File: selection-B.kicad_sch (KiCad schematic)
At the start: 5 parts, among them U14 74LS08, U15 74LS32, U16 74LS08, U17 74LS08, U18 74HC04

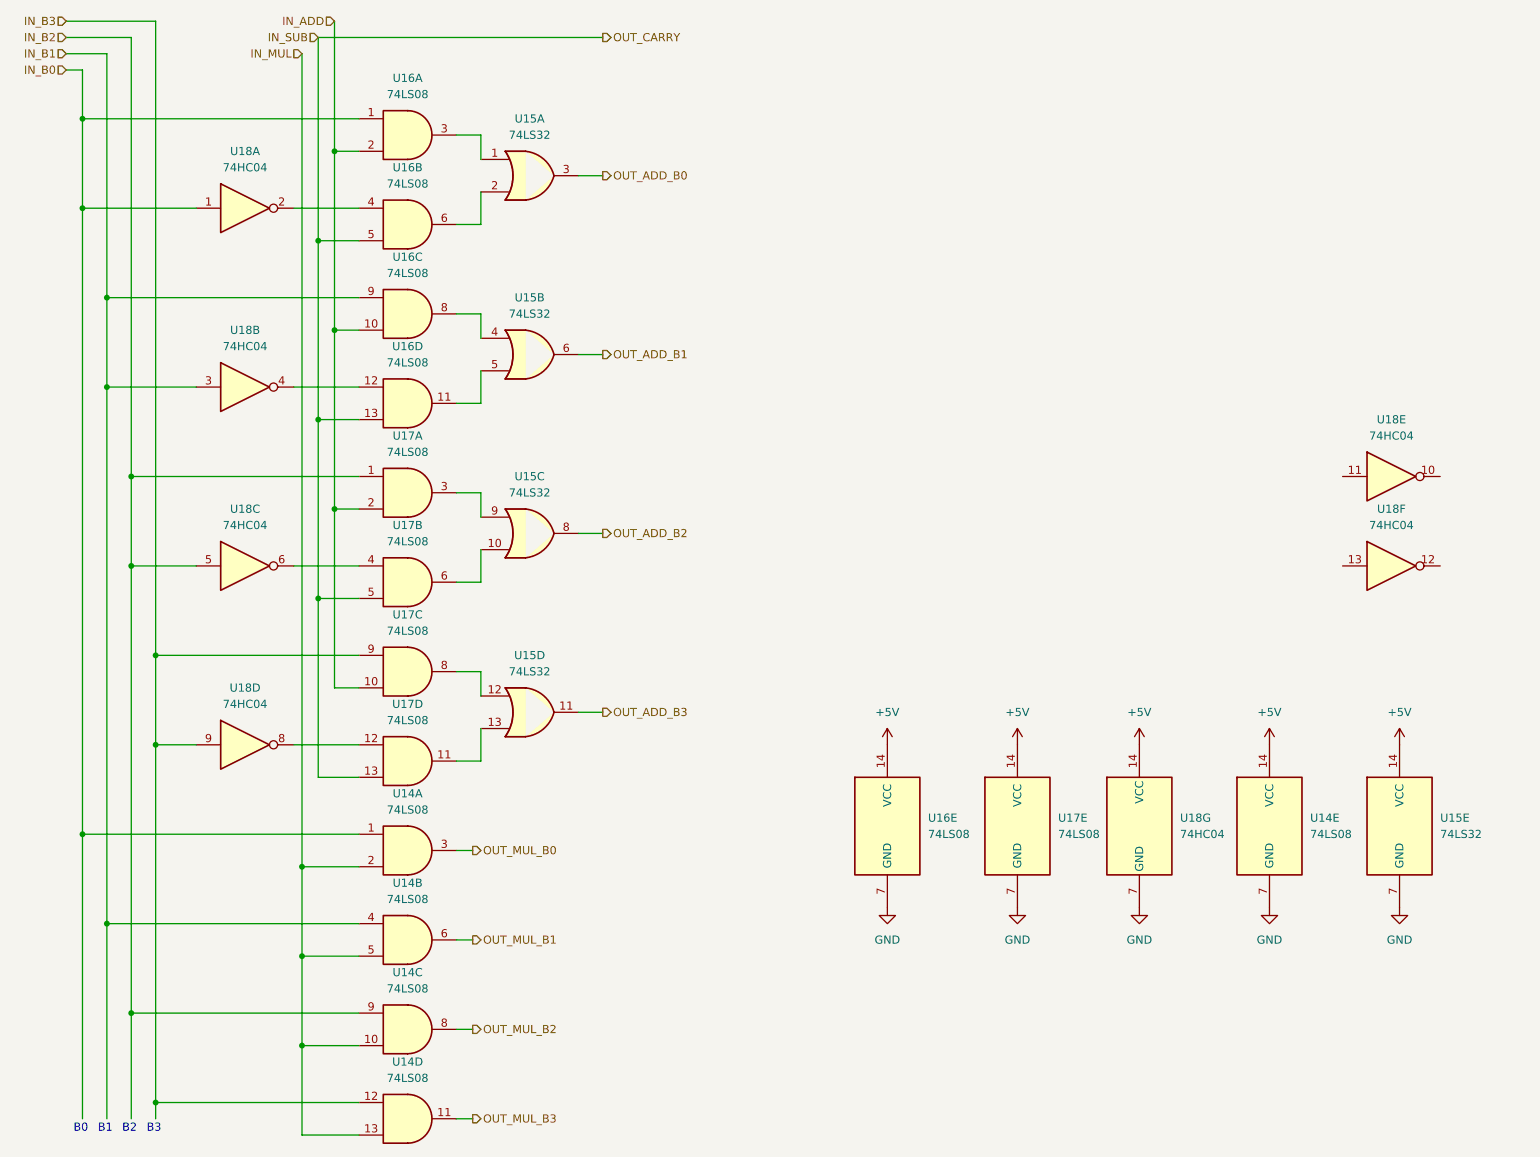
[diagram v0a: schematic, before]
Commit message: feat: removed ERC errors
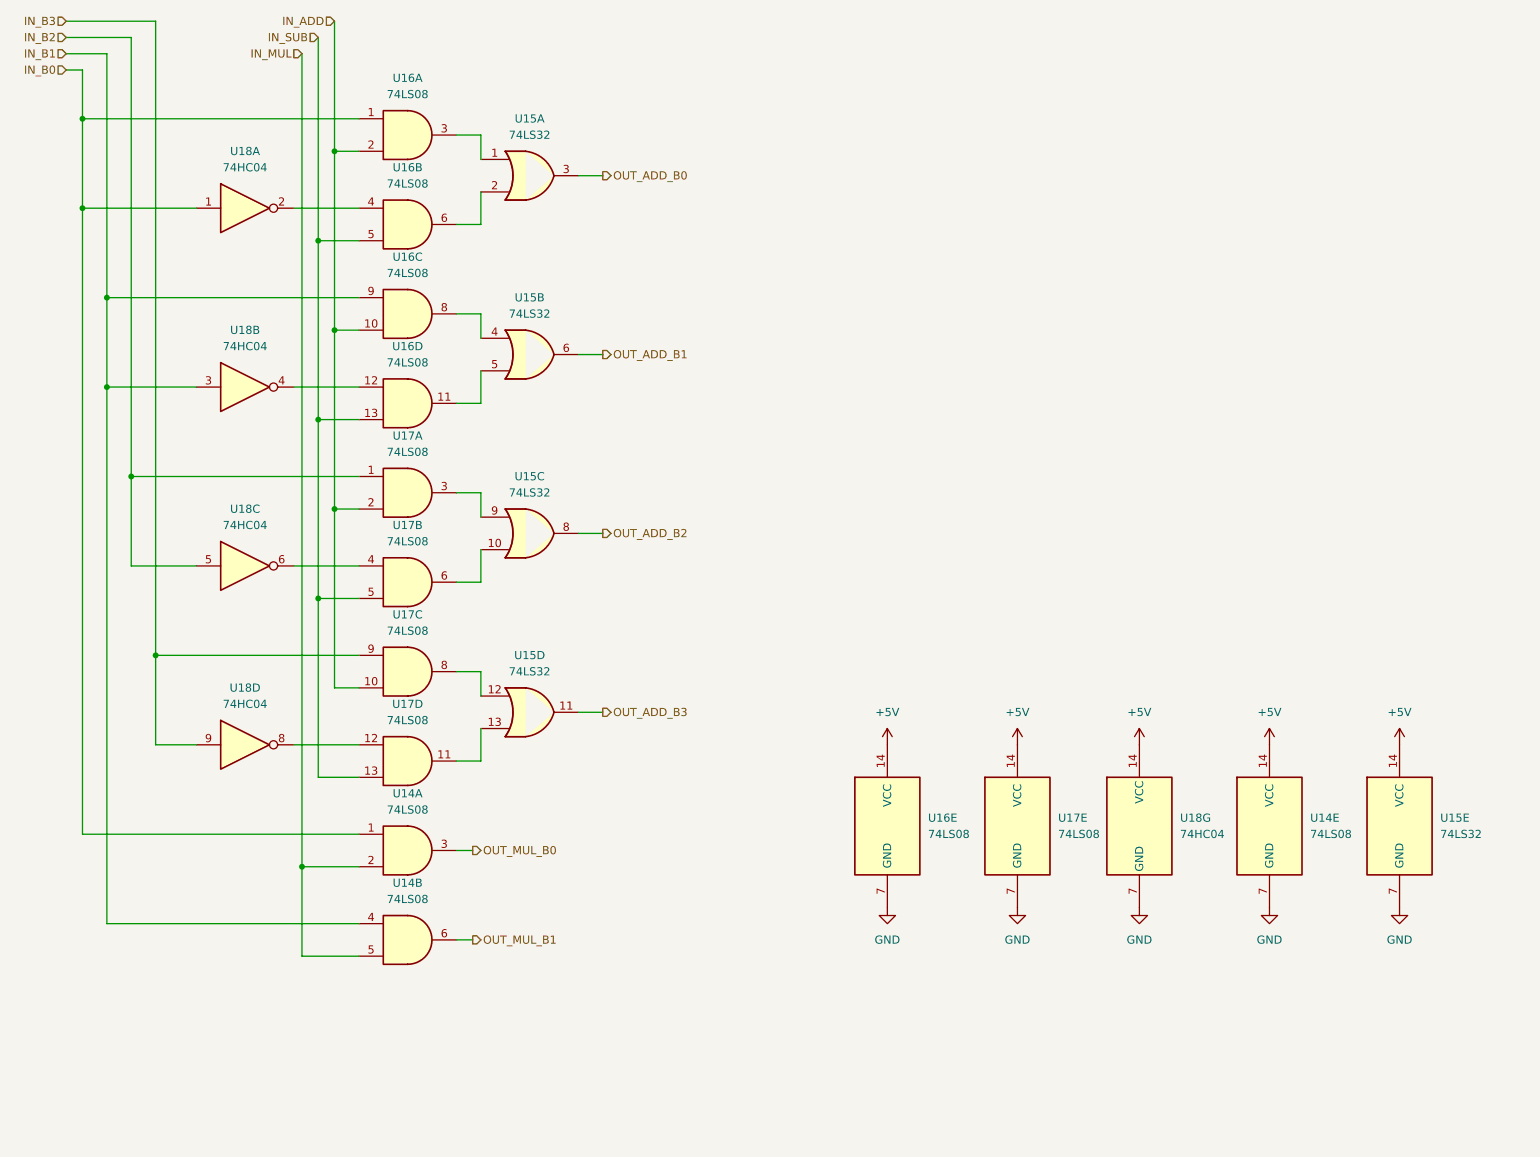
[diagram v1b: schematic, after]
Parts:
- removed unit 4 of U14
- removed unit 3 of U14
- removed unit 6 of U18
- removed unit 5 of U18
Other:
- note removed: "B0"
- note removed: "B1"
- note removed: "B2"
- note removed: "B3"

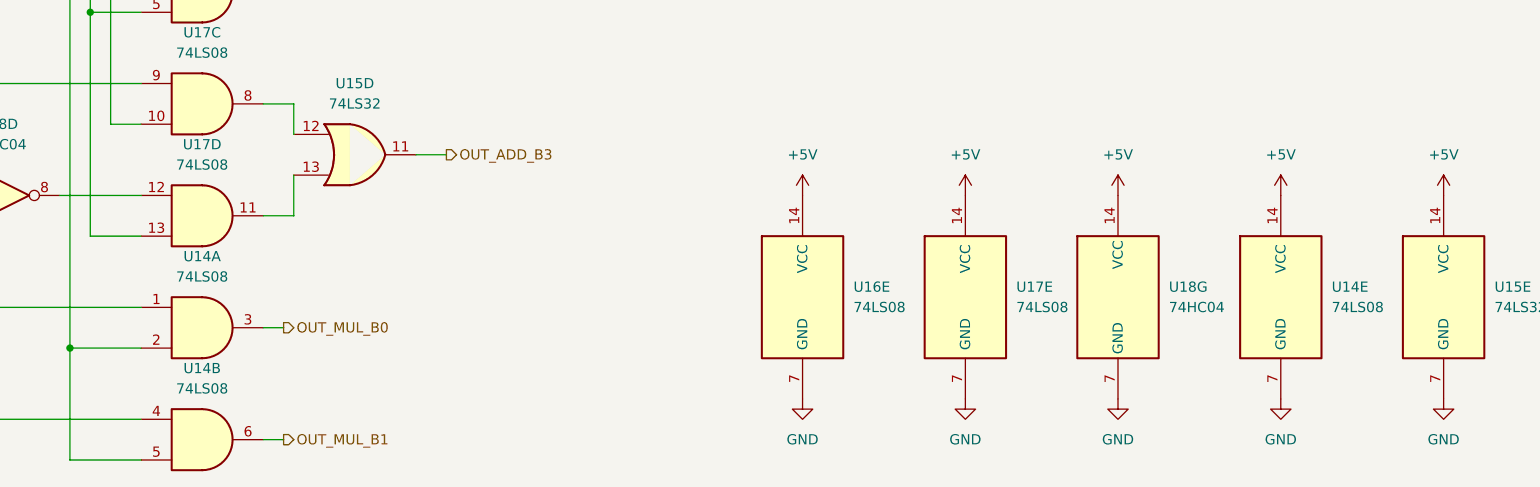
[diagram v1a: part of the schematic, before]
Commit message: fix: removed ERC warnings and errors
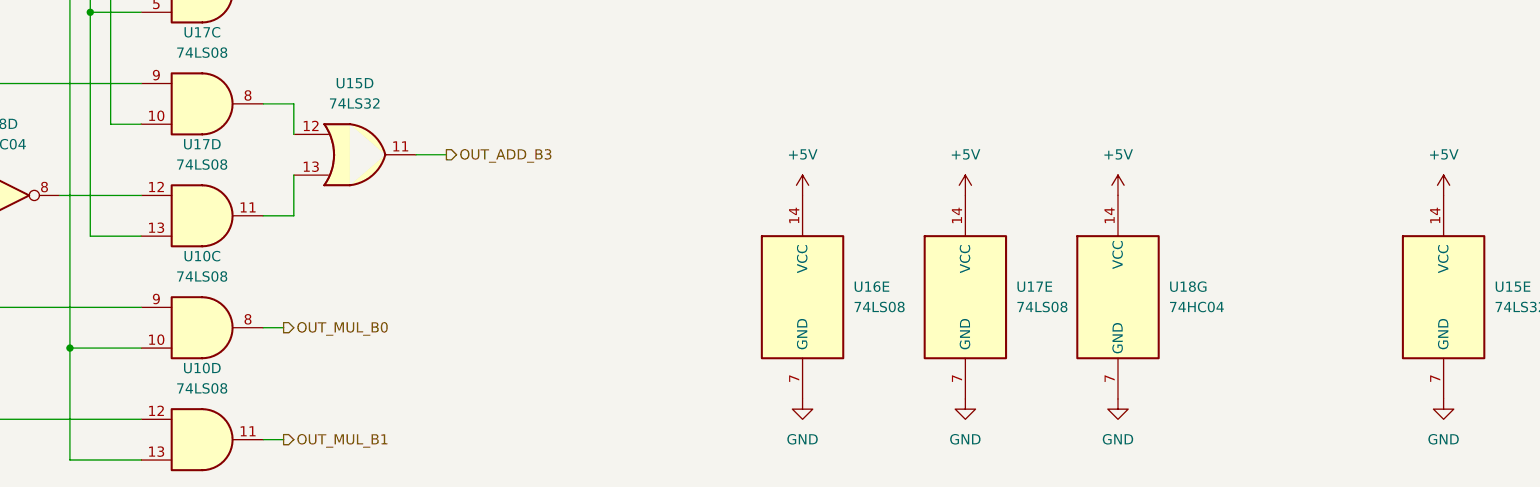
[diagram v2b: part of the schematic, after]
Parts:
- removed unit 5 of U14
- renumbered U14 to U10
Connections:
- net IN_B0: now also U10.9; no longer U10.1
- net IN_B1: now also U10.12; no longer U10.4
- net IN_MUL: now also U10.10, U10.13; no longer U10.2, U10.5
- net OUT_MUL_B0: now also U10.8; no longer U10.3
- net OUT_MUL_B1: now also U10.11; no longer U10.6
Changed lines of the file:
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@@
 		(lib_id "74xx:74LS08")
 		(at 113.03 161.29 0)
-		(unit 2)
-		(exclude_from_sim no)
-		(in_bom yes)
-		(on_board yes)
-		(dnp no)
-		(fields_autoplaced yes)
-		(property "Reference" "U14"
+		(unit 4)
+		(exclude_from_sim no)
+		(in_bom yes)
+		(on_board yes)
+		(dnp no)
+		(fields_autoplaced yes)
+		(property "Reference" "U10"
 			(at 113.0217 152.4 0)
 			(effects
@@
 			(project ""
 				(path "/4987240f-8890-46b8-b8e9-0d60580cb205/e08b8046-a666-4685-8ce4-06ee0f7f0287"
-					(reference "U14")
-					(unit 2)
+					(reference "U10")
+					(unit 4)
 				)
 			)
@@
 		(lib_id "74xx:74LS08")
 		(at 113.03 147.32 0)
-		(unit 1)
-		(exclude_from_sim no)
-		(in_bom yes)
-		(on_board yes)
-		(dnp no)
-		(fields_autoplaced yes)
-		(property "Reference" "U14"
+		(unit 3)
+		(exclude_from_sim no)
+		(in_bom yes)
+		(on_board yes)
+		(dnp no)
+		(fields_autoplaced yes)
+		(property "Reference" "U10"
 			(at 113.0217 138.43 0)
 			(effects
@@
 			(project ""
 				(path "/4987240f-8890-46b8-b8e9-0d60580cb205/e08b8046-a666-4685-8ce4-06ee0f7f0287"
-					(reference "U14")
-					(unit 1)
-				)
-			)
-		)
-	)
-	(symbol
-		(lib_id "74xx:74LS08")
-		(at 247.65 143.51 0)
-		(unit 5)
-		(exclude_from_sim no)
-		(in_bom yes)
-		(on_board yes)
-		(dnp no)
-		(fields_autoplaced yes)
-		(property "Reference" "U14"
-			(at 254 142.2399 0)
-			(effects
-				(font
-					(size 1.27 1.27)
-				)
-				(justify left)
-			)
-		)
-		(property "Value" "74LS08"
-			(at 254 144.7799 0)
-			(effects
-				(font
-					(size 1.27 1.27)
-				)
-				(justify left)
-			)
-		)
-		(property "Footprint" ""
-			(at 247.65 143.51 0)
-			(effects
-				(font
-					(size 1.27 1.27)
-				)
-				(hide yes)
-			)
-		)
-		(property "Datasheet" "http://www.ti.com/lit/gpn/sn74LS08"
-			(at 247.65 143.51 0)
-			(effects
-				(font
-					(size 1.27 1.27)
-				)
-				(hide yes)
-			)
-		)
-		(property "Description" "Quad And2"
-			(at 247.65 143.51 0)
-			(effects
-				(font
-					(size 1.27 1.27)
-				)
-				(hide yes)
-			)
-		)
-		(pin "2"
-		)
-		(pin "12"
-		)
-		(pin "9"
-		)
-		(pin "7"
-		)
-		(pin "11"
-		)
-		(pin "13"
-		)
-		(pin "1"
-		)
-		(pin "10"
-		)
-		(pin "14"
-		)
-		(pin "8"
-		)
-		(pin "4"
-		)
-		(pin "3"
-		)
-		(pin "6"
-		)
-		(pin "5"
-		)
-		(instances
-			(project ""
-				(path "/4987240f-8890-46b8-b8e9-0d60580cb205/e08b8046-a666-4685-8ce4-06ee0f7f0287"
-					(reference "U14")
-					(unit 5)
+					(reference "U10")
+					(unit 3)
 				)
 			)
@@
 	)
 	(symbol
-		(lib_id "power:+5V")
-		(at 247.65 130.81 0)
-		(unit 1)
-		(exclude_from_sim no)
-		(in_bom yes)
-		(on_board yes)
-		(dnp no)
-		(fields_autoplaced yes)
-		(property "Reference" "#PWR028"
-			(at 247.65 134.62 0)
-			(effects
-				(font
-					(size 1.27 1.27)
-				)
-				(hide yes)
-			)
-		)
-		(property "Value" "+5V"
-			(at 247.65 125.73 0)
-			(effects
-				(font
-					(size 1.27 1.27)
-				)
-			)
-		)
-		(property "Footprint" ""
-			(at 247.65 130.81 0)
-			(effects
-				(font
-					(size 1.27 1.27)
-				)
-				(hide yes)
-			)
-		)
-		(property "Datasheet" ""
-			(at 247.65 130.81 0)
-			(effects
-				(font
-					(size 1.27 1.27)
-				)
-				(hide yes)
-			)
-		)
-		(property "Description" "Power symbol creates a global label with name \"+5V\""
-			(at 247.65 130.81 0)
-			(effects
-				(font
-					(size 1.27 1.27)
-				)
-				(hide yes)
-			)
-		)
-		(pin "1"
-		)
-		(instances
-			(project ""
-				(path "/4987240f-8890-46b8-b8e9-0d60580cb205/e08b8046-a666-4685-8ce4-06ee0f7f0287"
-					(reference "#PWR028")
-					(unit 1)
-				)
-			)
-		)
-	)
-	(symbol
 		(lib_id "74xx:74LS32")
 		(at 132.08 69.85 0)
@@
 				)
 			)
-		)
-	)
-	(symbol
-		(lib_id "power:GND")
-		(at 247.65 156.21 0)
-		(unit 1)
-		(exclude_from_sim no)
-		(in_bom yes)
-		(on_board yes)
-		(dnp no)
-		(fields_autoplaced yes)
-		(property "Reference" "#PWR033"
-			(at 247.65 162.56 0)
-			(effects
-				(font
-					(size 1.27 1.27)
-				)
-				(hide yes)
-			)
-		)
-		(property "Value" "GND"
-			(at 247.65 161.29 0)
-			(effects
-				(font
-					(size 1.27 1.27)
-				)
-			)
-		)
-		(property "Footprint" ""
-			(at 247.65 156.21 0)
-			(effects
-				(font
-					(size 1.27 1.27)
-				)
-				(hide yes)
-			)
-		)
-		(property "Datasheet" ""
-			(at 247.65 156.21 0)
-			(effects
-				(font
-					(size 1.27 1.27)
-				)
-				(hide yes)
-			)
-		)
-		(property "Description" "Power symbol creates a global label with name \"GND\" , ground"
-			(at 247.65 156.21 0)
-			(effects
-				(font
-					(size 1.27 1.27)
-				)
-				(hide yes)
-			)
-		)
-		(pin "1"
-		)
-		(instances
-			(project ""
-				(path "/4987240f-8890-46b8-b8e9-0d60580cb205/e08b8046-a666-4685-8ce4-06ee0f7f0287"
-					(reference "#PWR033")
-					(unit 1)
-				)
-			)

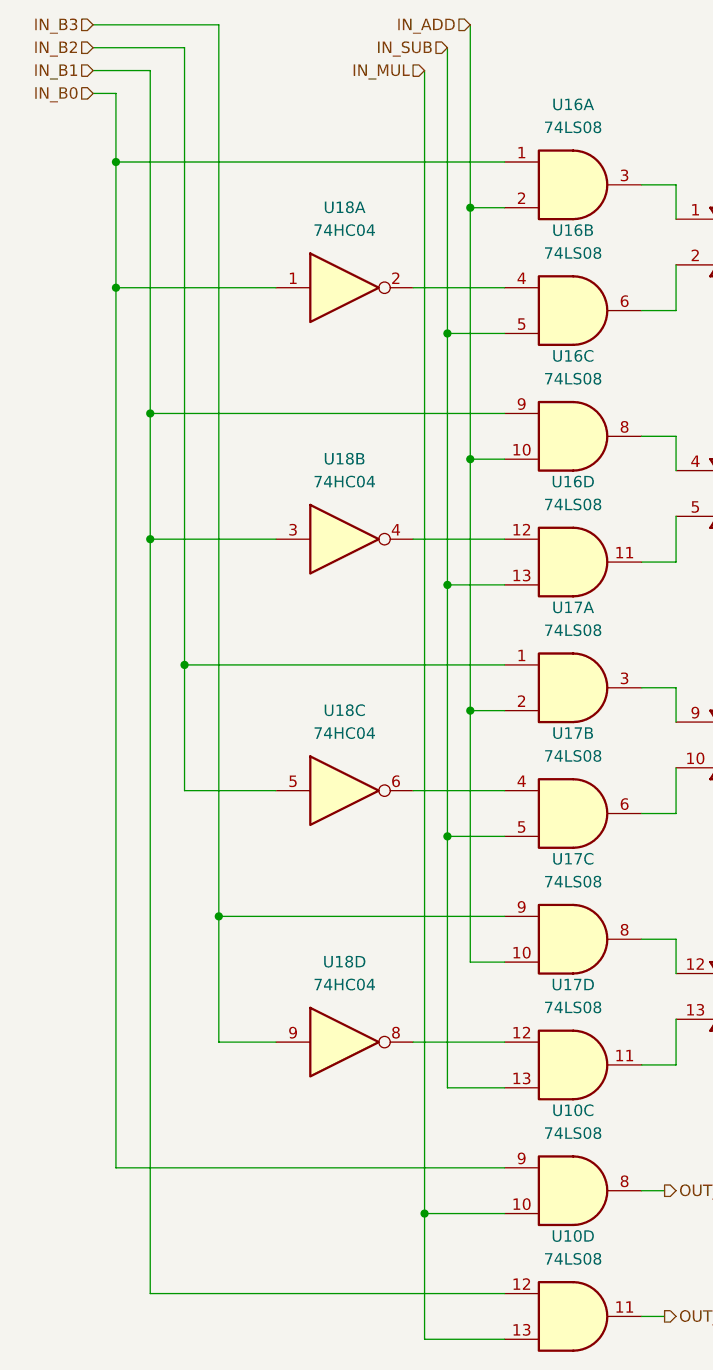
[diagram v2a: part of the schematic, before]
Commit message: feat: NOT to mofset + first batch of footprint
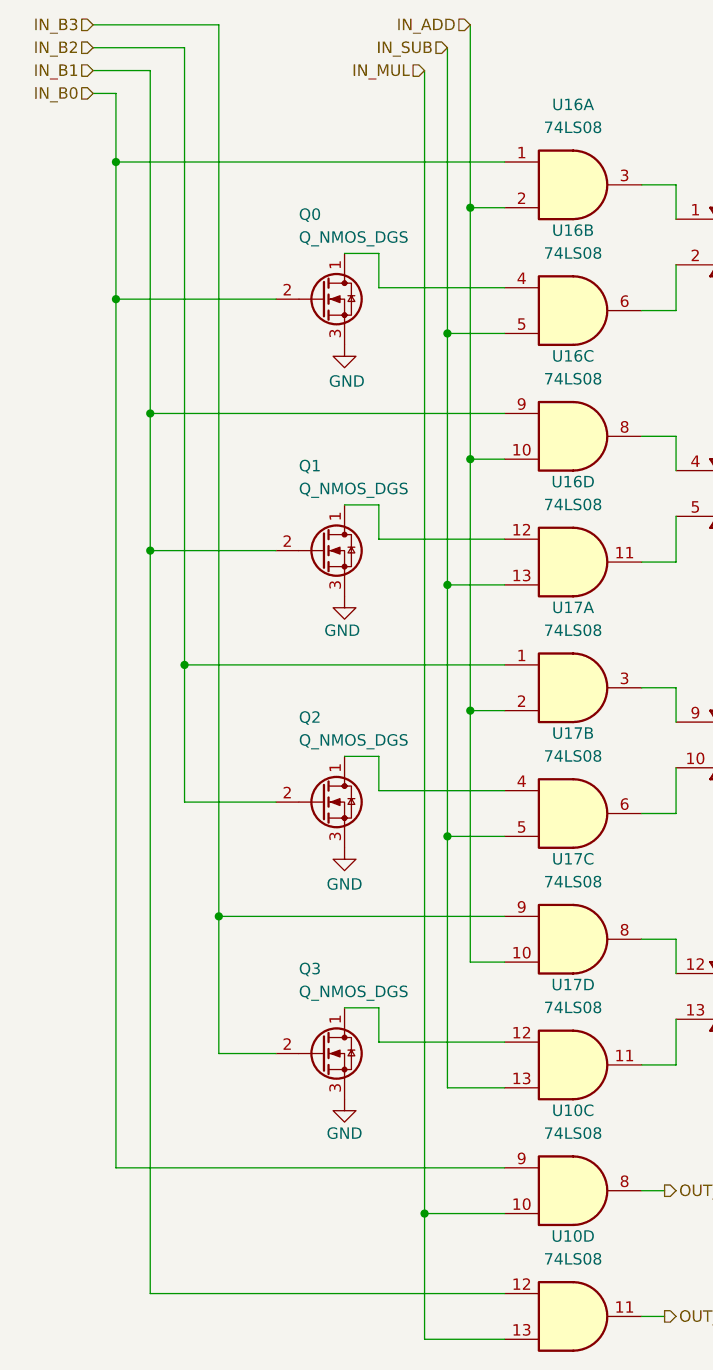
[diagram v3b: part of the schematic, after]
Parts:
- removed unit 3 of U18
- removed unit 4 of U18
- removed unit 1 of U18
- removed unit 2 of U18
- added Q0, Q1, Q2, Q3: Q_NMOS_DGS, symbol Transistor_FET:Q_NMOS_DGS
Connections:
- net GND: now also Q0.3 (S), Q1.3 (S), Q2.3 (S), Q3.3 (S)
- net IN_B0: now also Q0.2 (G)
- net IN_B1: now also Q1.2 (G)
- net IN_B2: now also Q2.2 (G)
- net IN_B3: now also Q3.2 (G)
- net at U17.4: now also Q2.1 (D)
- net at U17.12: now also Q3.1 (D)
- net at U16.12: now also Q1.1 (D)
- net at U16.4: now also Q0.1 (D)

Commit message: feat: added footprint for mofsets
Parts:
- Q0, Q1, Q2, Q3: footprint (none) -> Package_TO_SOT_SMD:SOT-23
